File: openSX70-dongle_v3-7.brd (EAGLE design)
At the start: 47.1 x 25.7 mm, 25 parts

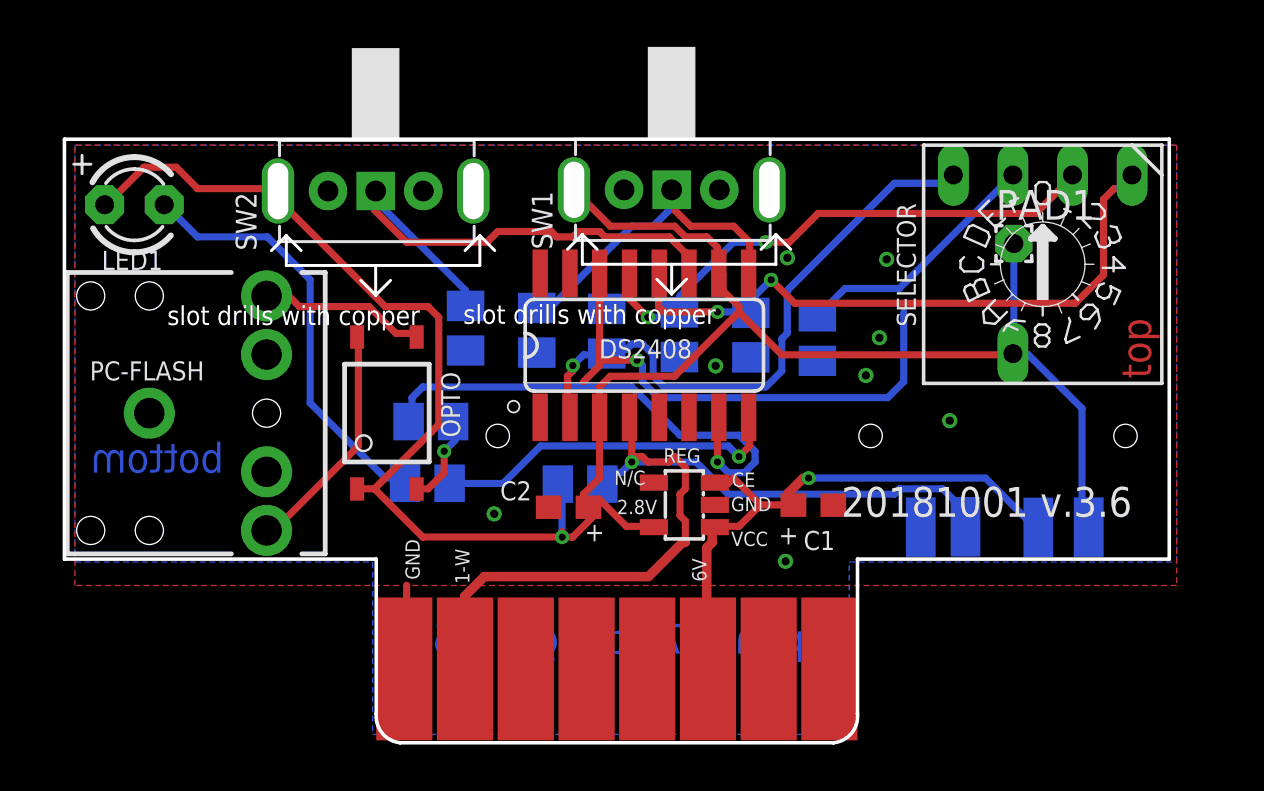
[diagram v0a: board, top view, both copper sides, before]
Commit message: New layout for 90º BCD
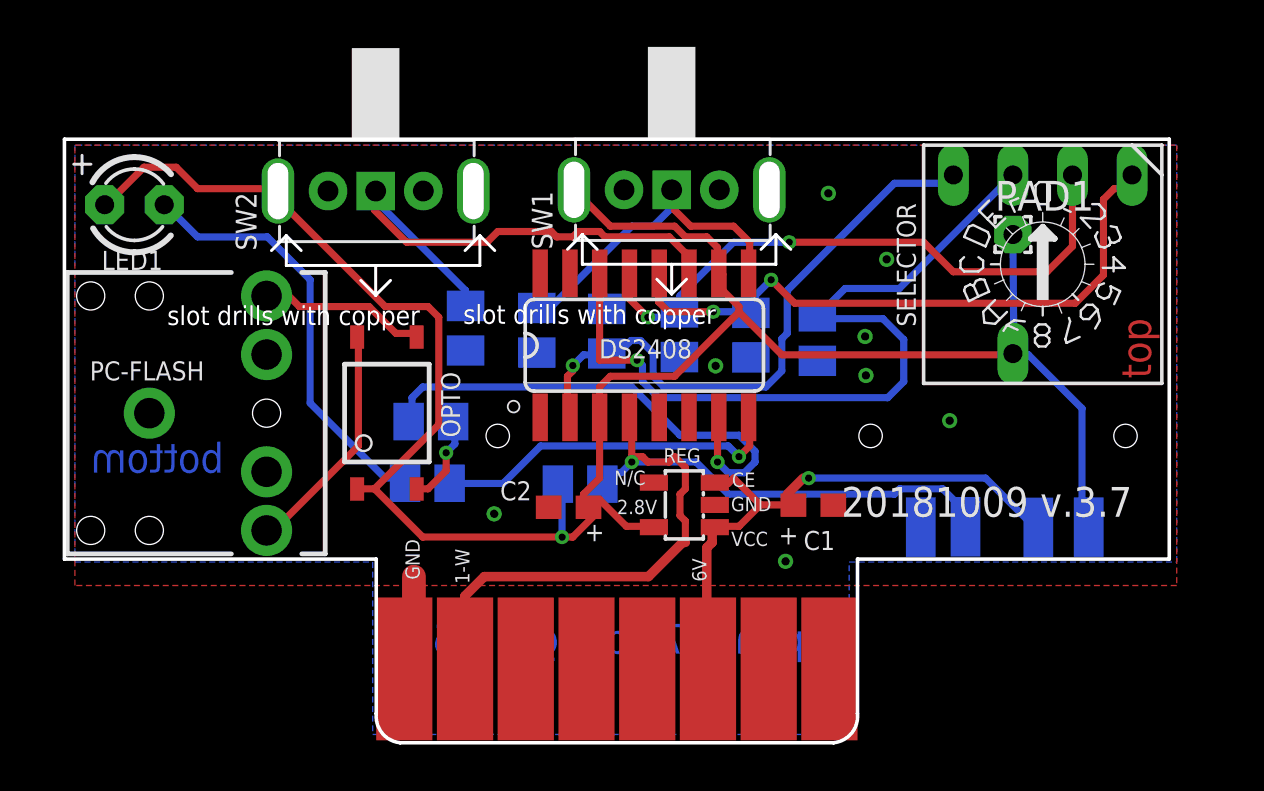
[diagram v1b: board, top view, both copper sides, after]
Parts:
- moved PAD1 0.39 mm to (42.5, 21.6)
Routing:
- net N$5: track 23.4 -> 26.2 mm
- net N$4: track 33.0 -> 34.8 mm
- net N$1: track 40.6 -> 39.1 mm
- net GND: track 3.60 -> 4.27 mm
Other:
- board text added: "20181009 v.3.7"
- board text removed: "20181001 v.3.6"

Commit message: 3.7 gerbers
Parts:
- renumbered LED1 to LED
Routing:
- net GND: track 4.27 -> 4.10 mm, vias 8 -> 3
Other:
- board text added: "1"
- board text added: "2"
- board text added: "openSX70 dongle 3.7"
- board text removed: "openSX70 dongle 3.6"

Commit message: ?
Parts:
- moved R3 0.22 mm to (34.2, 17.4)
- moved R8 0.22 mm to (19.2, 17.4)
- moved R7 0.13 mm to (22.2, 17.4)
- moved R2 0.09 mm to (25.2, 17.4)
- moved R9 0.08 mm to (17.6, 11.0)
- moved R12 0.08 mm to (17.6, 13.6)
- moved R5 0.08 mm to (31.4, 17.4)
- moved R4 0.06 mm to (28.3, 17.4)
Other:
- board text added: "20181106 v.3.8"
- board text removed: "20181009 v.3.7"
